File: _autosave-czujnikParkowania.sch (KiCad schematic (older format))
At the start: 44 parts, among them J1 Screw_Terminal_01x03, Q1 BC817, Q2 IRF7404, Q3 BC817, Q4 BC817, Q5 BC817, U1 DC56-11SEKWA, U2 LM7805_TO220, U3 HC-SR04, U4 ATmega328-AU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

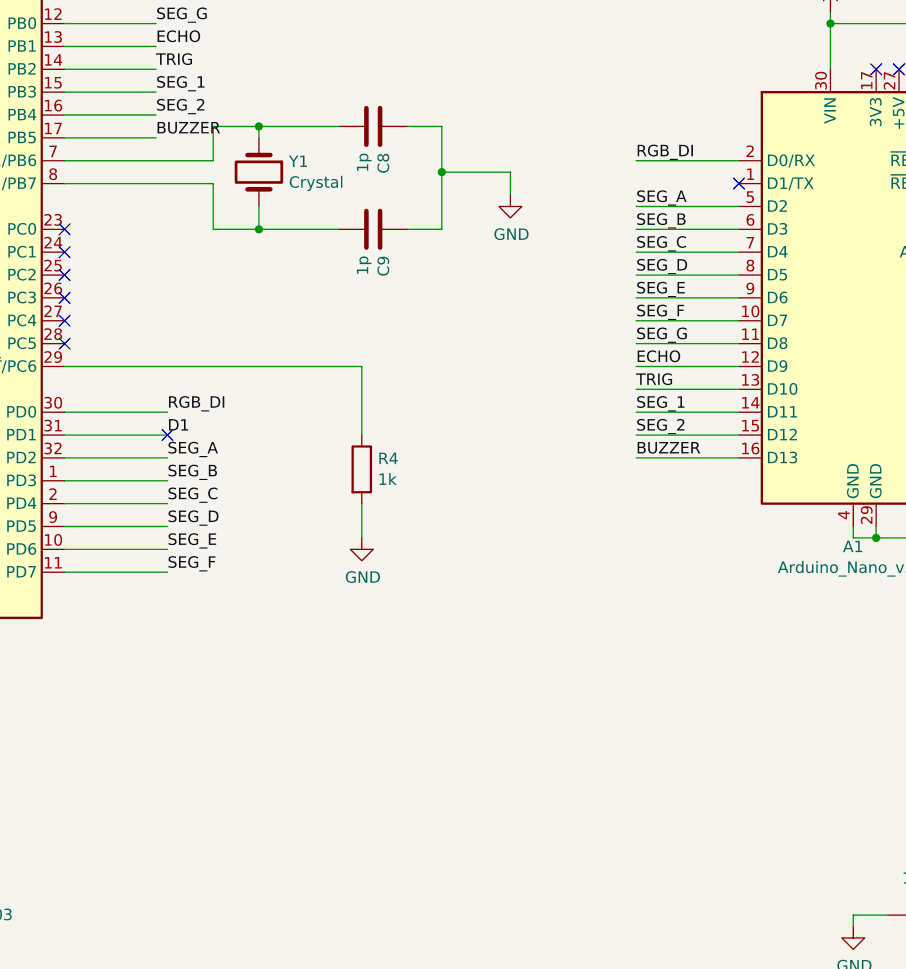
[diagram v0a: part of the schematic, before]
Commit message: Added button
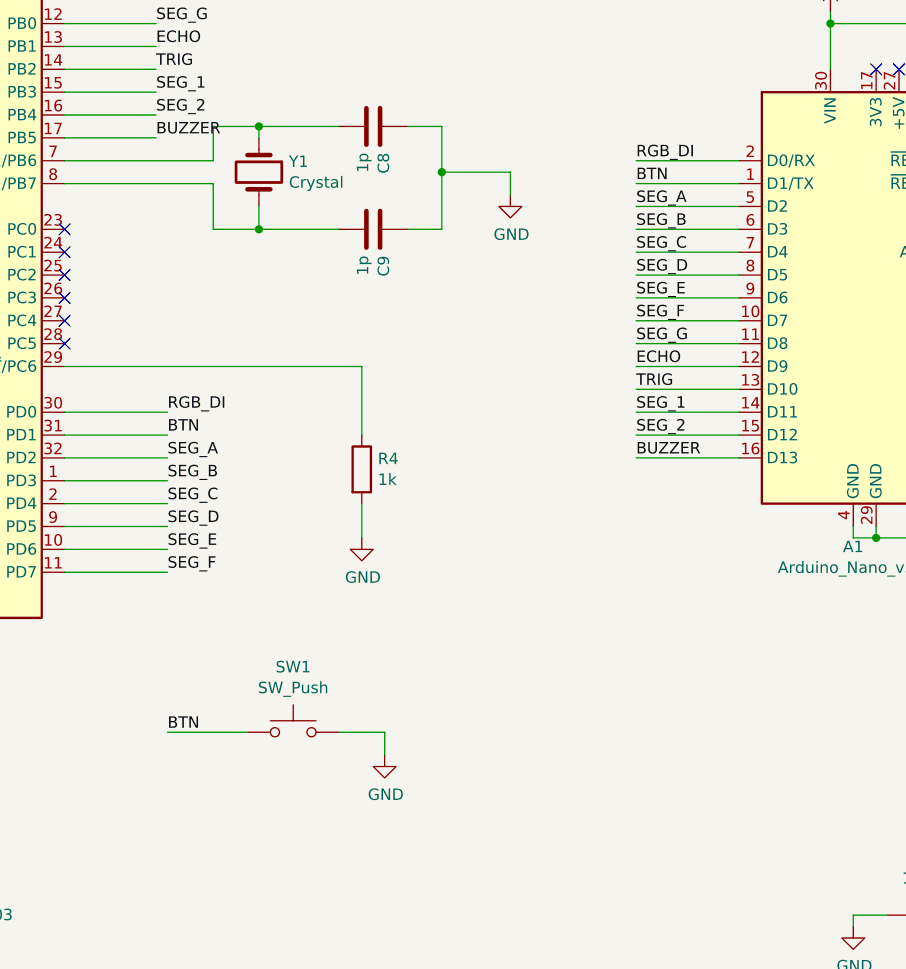
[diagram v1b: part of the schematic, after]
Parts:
- added SW1: SW_Push, Button_Switch_SMD:SW_SPST_B3S-1000, symbol Switch:SW_Push
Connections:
- net D1 is gone; now on net BTN: U4.31 (PD1)
- net GND: now also SW1.2
- net BTN: now reaches A1.1 (D1/TX)
- net BTN: now also SW1.1
- no-connect marks 23 -> 21
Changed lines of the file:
@@
 RGB_DI
 Text Label 3150 3050 0    50   ~ 0
-D1
+BTN
 Text Label 3150 3150 0    50   ~ 0
 SEG_A
@@
 Text Label 3100 1750 0    50   ~ 0
 BUZZER
-NoConn ~ 3150 3050
 $Comp
 L MCU_Module:Arduino_Nano_v3.x A1
@@
 NoConn ~ 6650 3050
 NoConn ~ 6650 3150
-NoConn ~ 5650 1950
 $Comp
 L power:+5V #PWR0107
@@
 Text Label 5200 3150 0    50   ~ 0
 BUZZER
+$Comp
+L Switch:SW_Push SW1
+U 1 1 5EA69D05
+P 3700 4350
+F 0 "SW1" H 3700 4635 50  0000 C CNN
+F 1 "SW_Push" H 3700 4544 50  0000 C CNN
+F 2 "Button_Switch_SMD:SW_SPST_B3S-1000" H 3700 4550 50  0001 C CNN
+F 3 "https://www.tme.eu/pl/details/b3s-1000/mikroprzelaczniki-tact/omron-ocb/" H 3700 4550 50  0001 C CNN
+	1    3700 4350
+	1    0    0    -1
+$EndComp
+Wire Wire Line
+	5650 1950 5200 1950
+Text Label 5200 1950 0    50   ~ 0
+BTN
+Wire Wire Line
+	3500 4350 3150 4350
+$Comp
+L power:GND #PWR0129
+U 1 1 5EAA1D9B
+P 4100 4450
+F 0 "#PWR0129" H 4100 4200 50  0001 C CNN
+F 1 "GND" H 4105 4277 50  0000 C CNN
+F 2 "" H 4100 4450 50  0001 C CNN
+F 3 "" H 4100 4450 50  0001 C CNN
+	1    4100 4450
+	1    0    0    -1
+$EndComp
+Wire Wire Line
+	3900 4350 4100 4350
+Wire Wire Line
+	4100 4350 4100 4450
+Text Label 3150 4350 0    50   ~ 0
+BTN
 $EndSCHEMATC
